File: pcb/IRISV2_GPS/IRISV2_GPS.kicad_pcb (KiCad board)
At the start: 4 copper layers, 50 x 50 mm, 27 parts, among them J1 Conn_01x06_MountingPin, U1 NEO-M9N, U2 lna

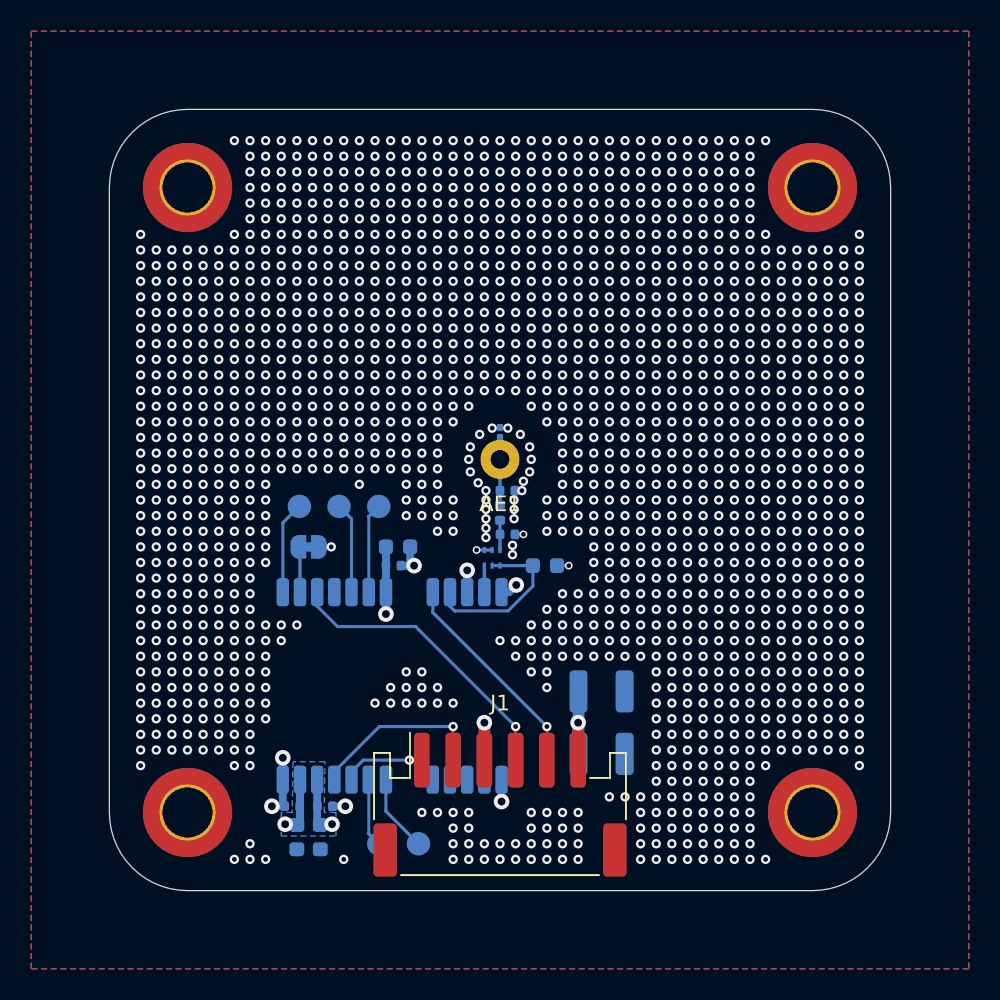
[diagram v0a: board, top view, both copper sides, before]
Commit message: fixed some issues, lr2021 matching is now 0201 - todo change trace width to match pad width like ref design, see todo for rest
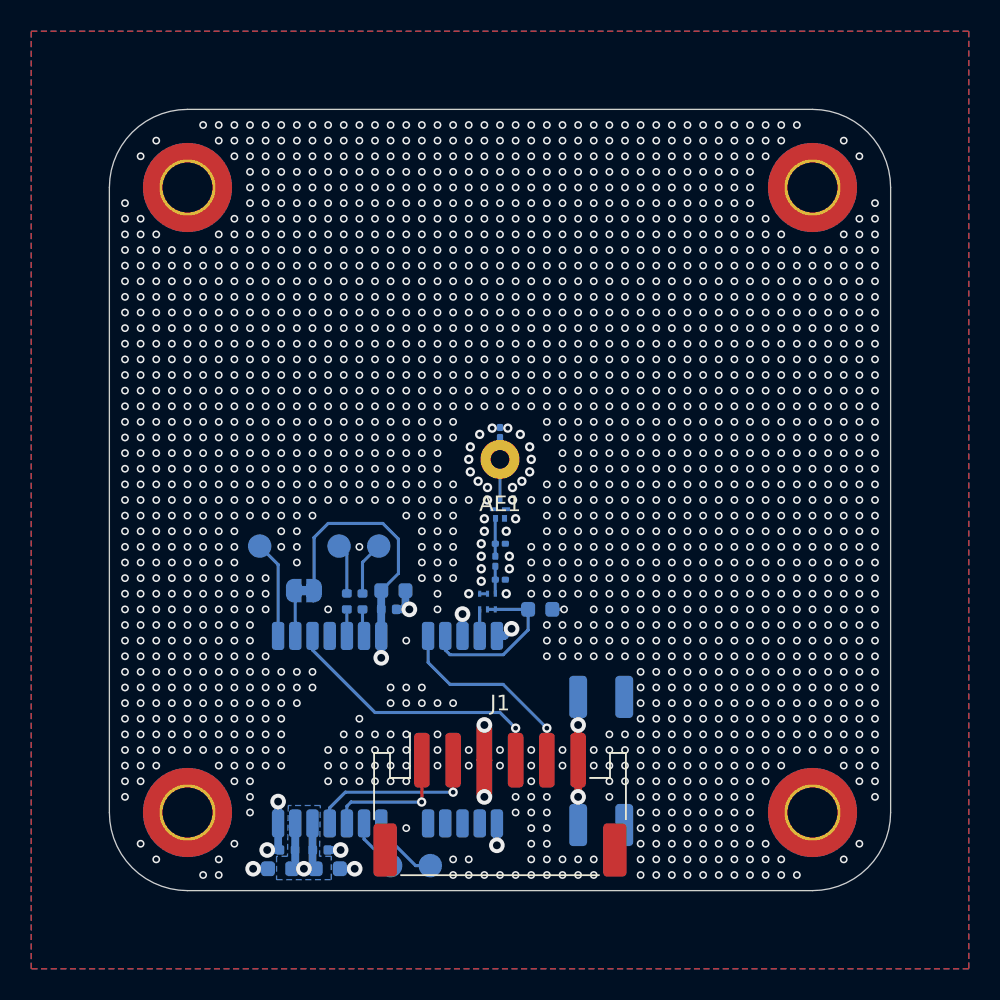
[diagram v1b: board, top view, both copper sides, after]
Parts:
- removed D+: GPS_D+, TestPoint:TestPoint_Pad_D1.5mm
- removed D-: GPS_D-, TestPoint:TestPoint_Pad_D1.5mm
- added FL1: AFII-SW-0061-T, AFII-SW-0061-T:AFIISW0061T, B.Cu at (150.0, 105.6)
- added R1: 22, Resistor_SMD:R_0402_1005Metric, B.Cu at (140.2, 111.5)
- added R2: 22, Resistor_SMD:R_0402_1005Metric, B.Cu at (141.2, 111.5)
- added TP1: GPS_D-, TestPoint:TestPoint_Pad_D1.5mm, B.Cu at (139.7, 108.0)
- added TP2: GPS_D+, TestPoint:TestPoint_Pad_D1.5mm, B.Cu at (142.2, 108.0)
- C10, C11: footprint Capacitor_SMD:C_0402_1005Metric -> Capacitor_SMD:C_0201_0603Metric
- L1: footprint Inductor_SMD:L_0402_1005Metric -> Inductor_SMD:L_0201_0603Metric
- moved C1 4.55 mm to (156.5, 125.8)
- moved BOOT 3.59 mm to (134.6, 108.0)
- moved C11 3.43 mm to (150.0, 107.8)
- moved L1 3.12 mm to (149.7, 108.9)
- moved C10 2.94 mm to (150.0, 110.1)
- moved C8 2.82 mm to (138.5, 127.4)
- moved C6 2.82 mm to (136.4, 127.4)
- moved C7 2.82 mm to (142.9, 112.0)
- moved C9 2.82 mm to (152.6, 112.0)
- moved DSEL 2.82 mm to (137.4, 110.8)
- moved U2 2.82 mm to (149.2, 111.5)
- moved C4 2.82 mm to (143.2, 110.8)
- moved U1 2.82 mm to (142.8, 119.7)
- moved C3 2.29 mm to (135.9, 128.6), turned to 180 degrees
- moved C5 2.08 mm to (139.0, 128.6), turned to 0 degrees
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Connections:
- C11 pad 1: Net-(AE1-A) -> Net-(FL1-OUTPUT)
- L1 pad 2: Net-(AE1-A) -> Net-(FL1-OUTPUT)
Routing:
- net +3.3V: track 33.6 -> 65.8 mm, vias 5 -> 4
- net Net-(U1-USB_DM): track 5.82 -> 1.70 mm
- net Net-(U1-USB_DP): track 5.76 -> 1.74 mm
- net Net-(R2-Pad2): track 0.00 -> 3.46 mm
- net gps_mrx: track 5.32 -> 8.68 mm
- net Net-(R1-Pad1): track 0.00 -> 3.24 mm
- net GND: track 15.6 -> 18.6 mm, vias 1567 -> 1833
- net Net-(FL1-OUTPUT): track 0.00 -> 2.43 mm
- net Net-(U1-SCL/SPI_CLK): track 4.37 -> 3.40 mm
- net gps_pps: track 18.9 -> 18.0 mm
- net gps_rst: track 13.8 -> 13.1 mm
- removed copper zone on In1.Cu, net +3.3V

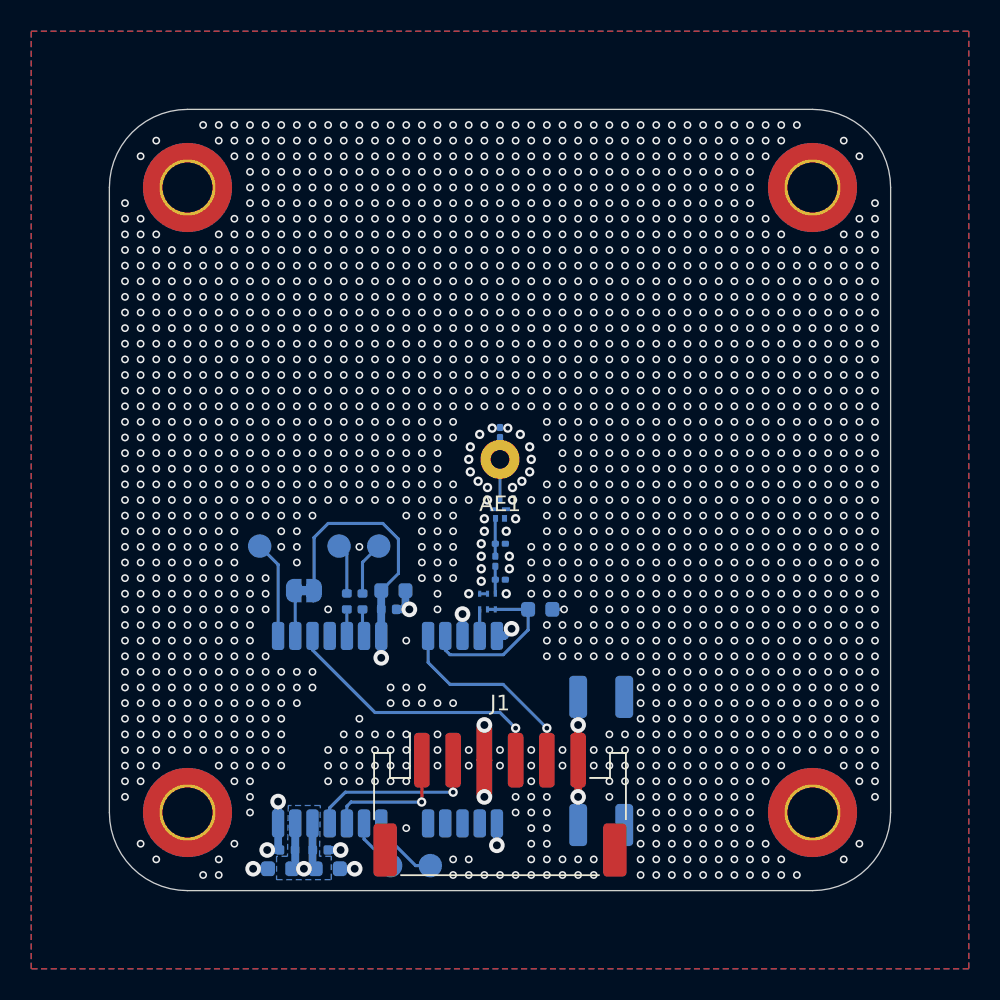
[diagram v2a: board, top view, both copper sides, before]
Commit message: 3d models nearly done, just missing a few, gpio header routed - about to change lr2021 trace width
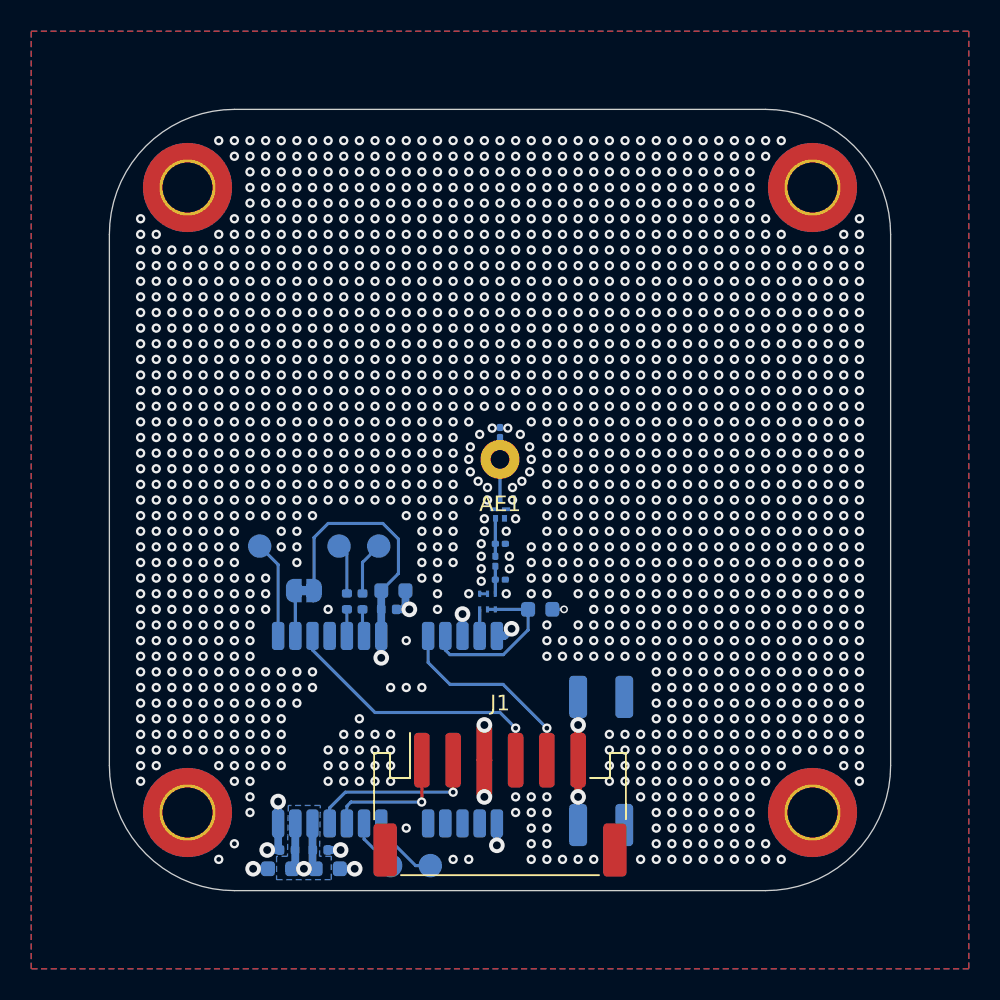
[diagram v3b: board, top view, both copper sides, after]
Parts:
- renumbered TP2 to D+, TP1 to D-
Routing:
- net GND: vias 1833 -> 1655
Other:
- outline, holes or cut-outs redrawn
